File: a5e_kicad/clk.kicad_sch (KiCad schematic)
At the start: 20 parts, among them J1601 Conn_01x03_Pin, U1601 5P49V60A0000NL, Y1601 FOX FQ5225B-25

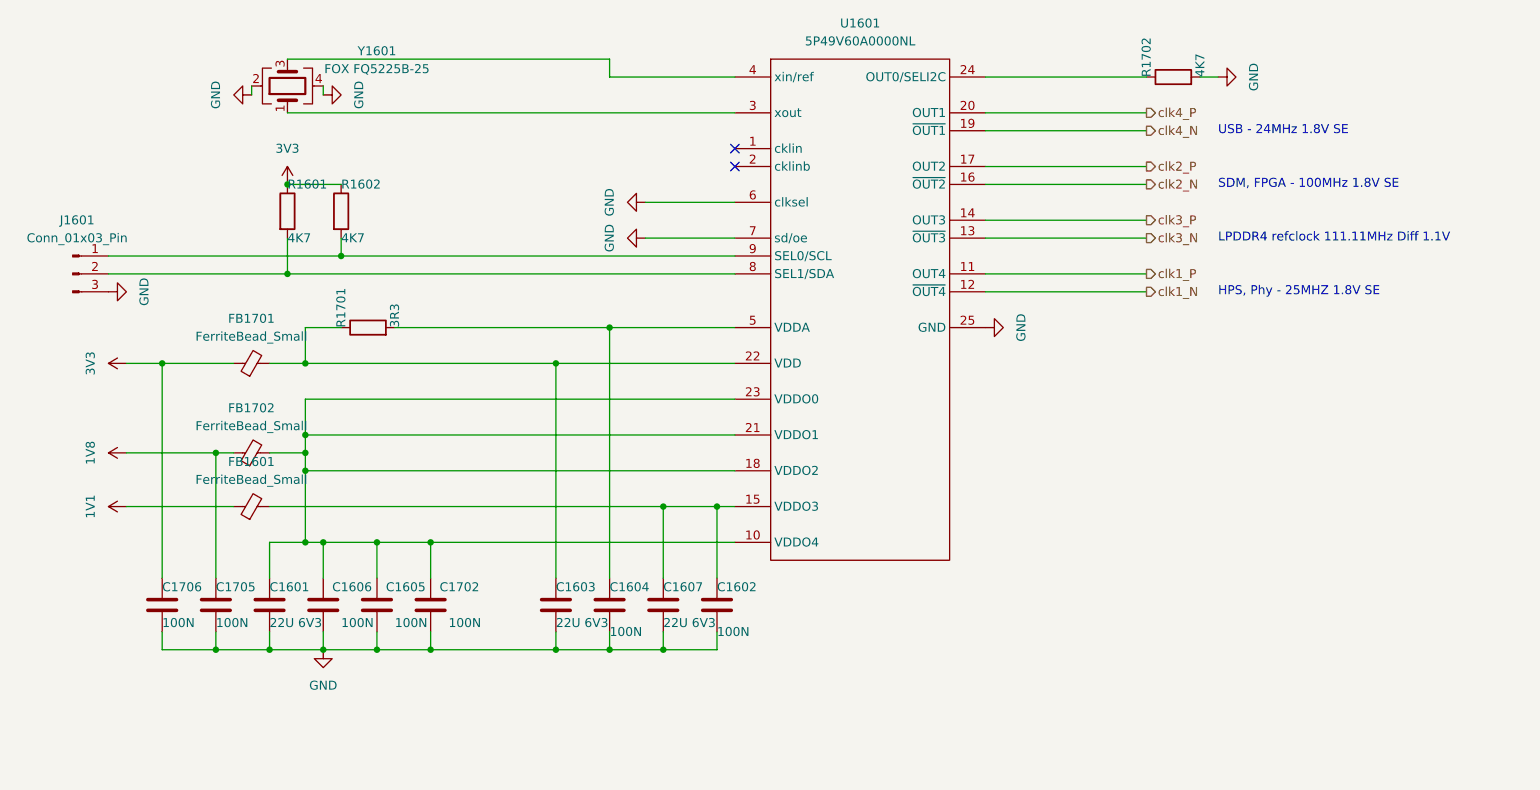
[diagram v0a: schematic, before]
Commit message: add vias to lppdr balls
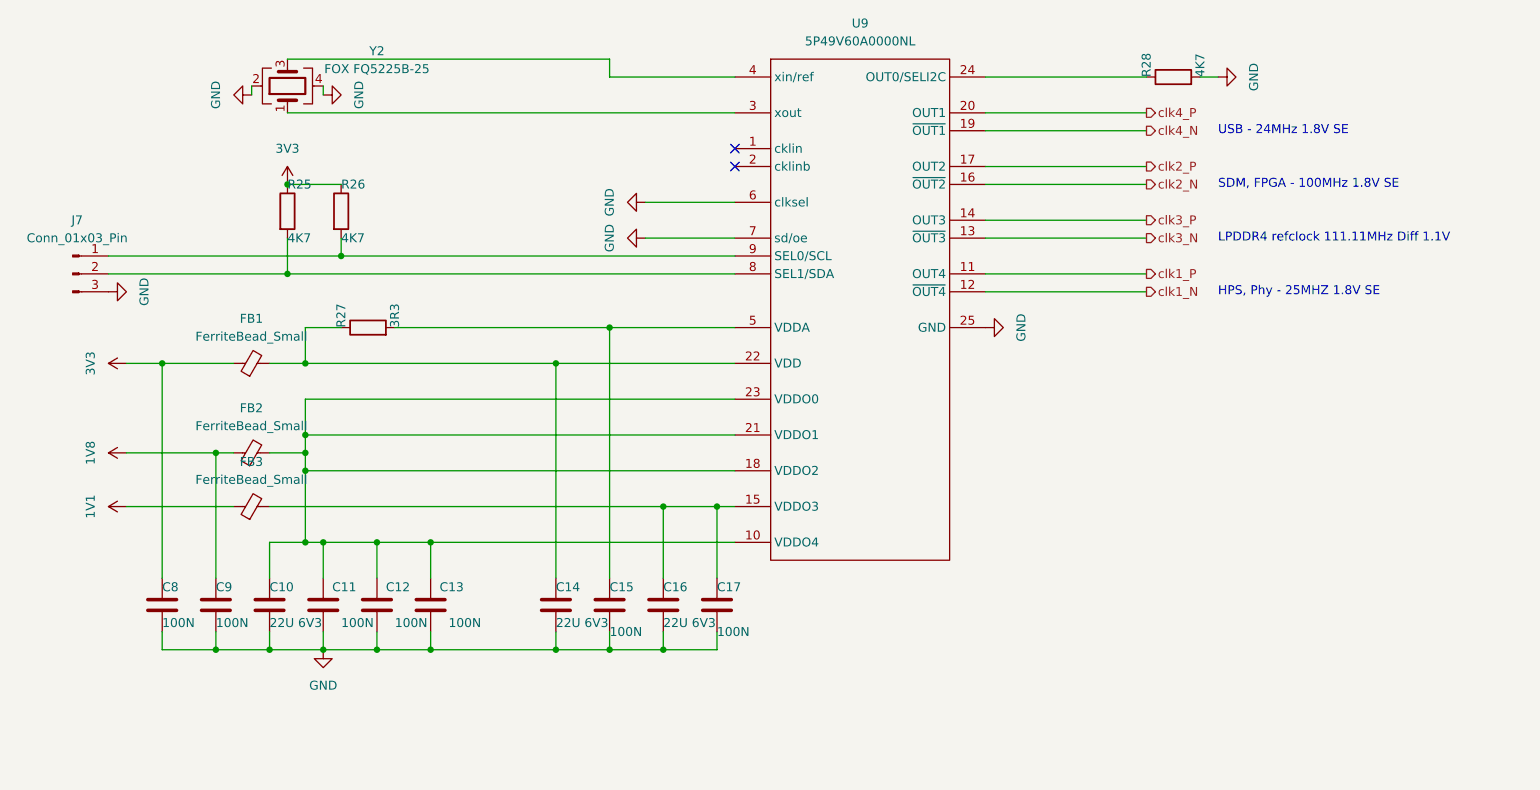
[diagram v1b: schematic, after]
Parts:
- renumbered C1601 to C10, C1606 to C11, C1605 to C12, C1702 to C13, C1603 to C14, C1604 to C15, C1607 to C16, C1602 to C17, C1706 to C8, C1705 to C9, FB1701 to FB1, FB1702 to FB2, FB1601 to FB3, J1601 to J7, R1601 to R25, R1602 to R26, R1701 to R27, R1702 to R28, U1601 to U9, Y1601 to Y2

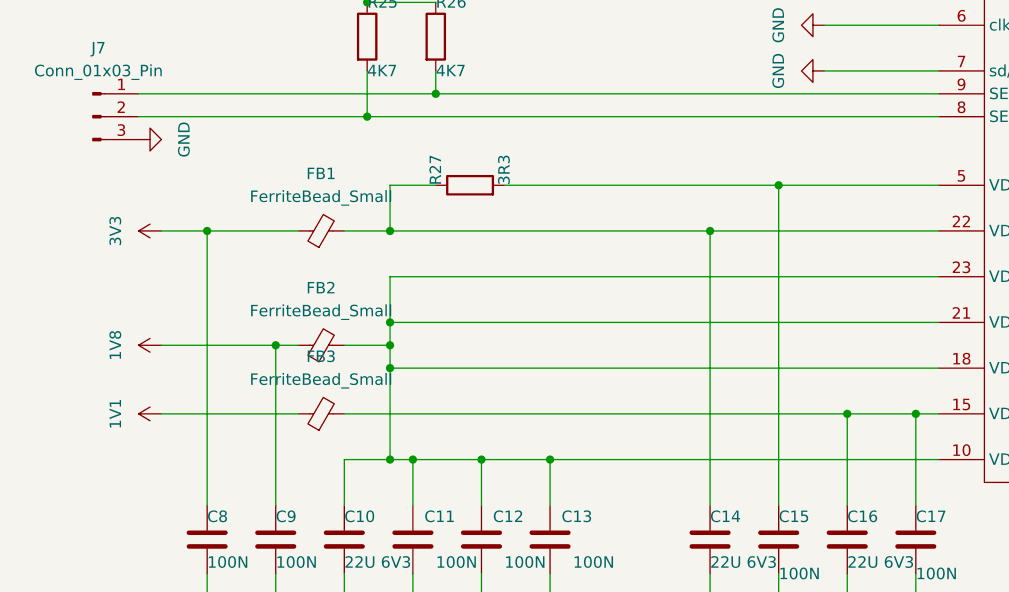
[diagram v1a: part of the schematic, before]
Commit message: add routes for power supplies
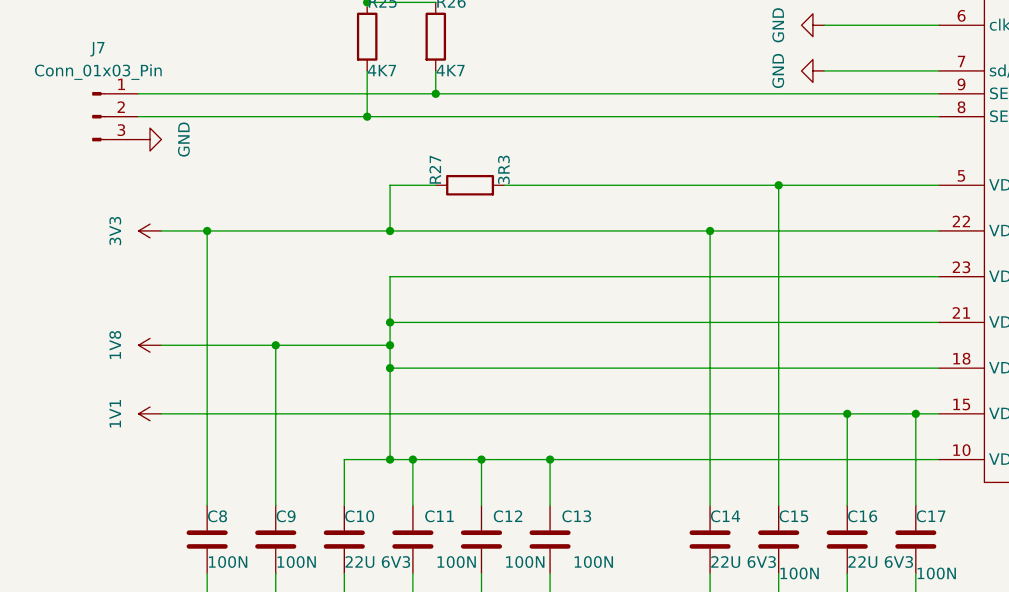
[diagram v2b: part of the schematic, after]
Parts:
- removed FB1, FB2, FB3: FerriteBead_Small, Capacitor_SMD:C_0603_1608Metric, symbol Device:FerriteBead_Small
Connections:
- net 1V1: now also C16.1, C17.1, U9.15 (VDDO3)
- net 1V8: now also C10.1, C11.1, C12.1, C13.1, U9.10 (VDDO4), U9.18 (VDDO2), U9.21 (VDDO1), U9.23 (VDDO0)
- net 3V3: now also C14.1, R27.1, U9.22 (VDD)

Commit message: savegame before trying to fix component names
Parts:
- added Y3: Si5351B-B-GM, Package_DFN_QFN:QFN-20-1EP_4x4mm_P0.5mm_EP2.7x2.7mm, symbol Oscillator:Si5351B-B-GM
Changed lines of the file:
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@@
+	)
+	(symbol
+		(lib_id "Oscillator:Si5351B-B-GM")
+		(at 212.09 113.03 0)
+		(unit 1)
+		(body_style 1)
+		(exclude_from_sim no)
+		(in_bom yes)
+		(on_board yes)
+		(in_pos_files yes)
+		(dnp no)
+		(fields_autoplaced yes)
+		(property "Reference" "Y3"
+			(at 214.2333 135.89 0)
+			(show_name no)
+			(do_not_autoplace no)
+			(effects
+				(font
+					(size 1.27 1.27)
+				)
+				(justify left)
+			)
+		)
+		(property "Value" "Si5351B-B-GM"
+			(at 214.2333 138.43 0)
+			(show_name no)
+			(do_not_autoplace no)
+			(effects
+				(font
+					(size 1.27 1.27)
+				)
+				(justify left)
+			)
+		)
+		(property "Footprint" "Package_DFN_QFN:QFN-20-1EP_4x4mm_P0.5mm_EP2.7x2.7mm"
+			(at 212.09 143.51 0)
+			(hide yes)
+			(show_name no)
+			(do_not_autoplace no)
+			(effects
+				(font
+					(size 1.27 1.27)
+				)
+			)
+		)
+		(property "Datasheet" "https://www.silabs.com/documents/public/data-sheets/Si5351-B.pdf"
+			(at 212.09 113.03 0)
+			(hide yes)
+			(show_name no)
+			(do_not_autoplace no)
+			(effects
+				(font
+					(size 1.27 1.27)
+				)
+			)
+		)
+		(property "Description" "I2C Programmable Any-Frequency CMOS Clock Generator + VCXO, QFN-20"
+			(at 212.09 113.03 0)
+			(hide yes)
+			(show_name no)
+			(do_not_autoplace no)
+			(effects
+				(font
+					(size 1.27 1.27)
+				)
+			)
+		)
+		(pin "2"
+		)
+		(pin "18"
+		)
+		(pin "21"
+		)
+		(pin "14"
+		)
+		(pin "6"
+		)
+		(pin "9"
+		)
+		(pin "1"
+		)
+		(pin "13"
+		)
+		(pin "10"
+		)
+		(pin "11"
+		)
+		(pin "5"
+		)
+		(pin "12"
+		)
+		(pin "16"
+		)
+		(pin "4"
+		)
+		(pin "15"
+		)
+		(pin "7"
+		)
+		(pin "3"
+		)
+		(pin "17"
+		)
+		(pin "19"
+		)
+		(pin "8"
+		)
+		(pin "20"
+		)
+		(instances
+			(project "agilex_3_soc"
+				(path "/a5b98d95-6877-4284-904f-d04e32723ae0/03ab2536-81c4-4b58-8998-1457d6fb7a1b"
+					(reference "Y3")
+					(unit 1)
+				)
+			)
+		)
 	)
 	(symbol

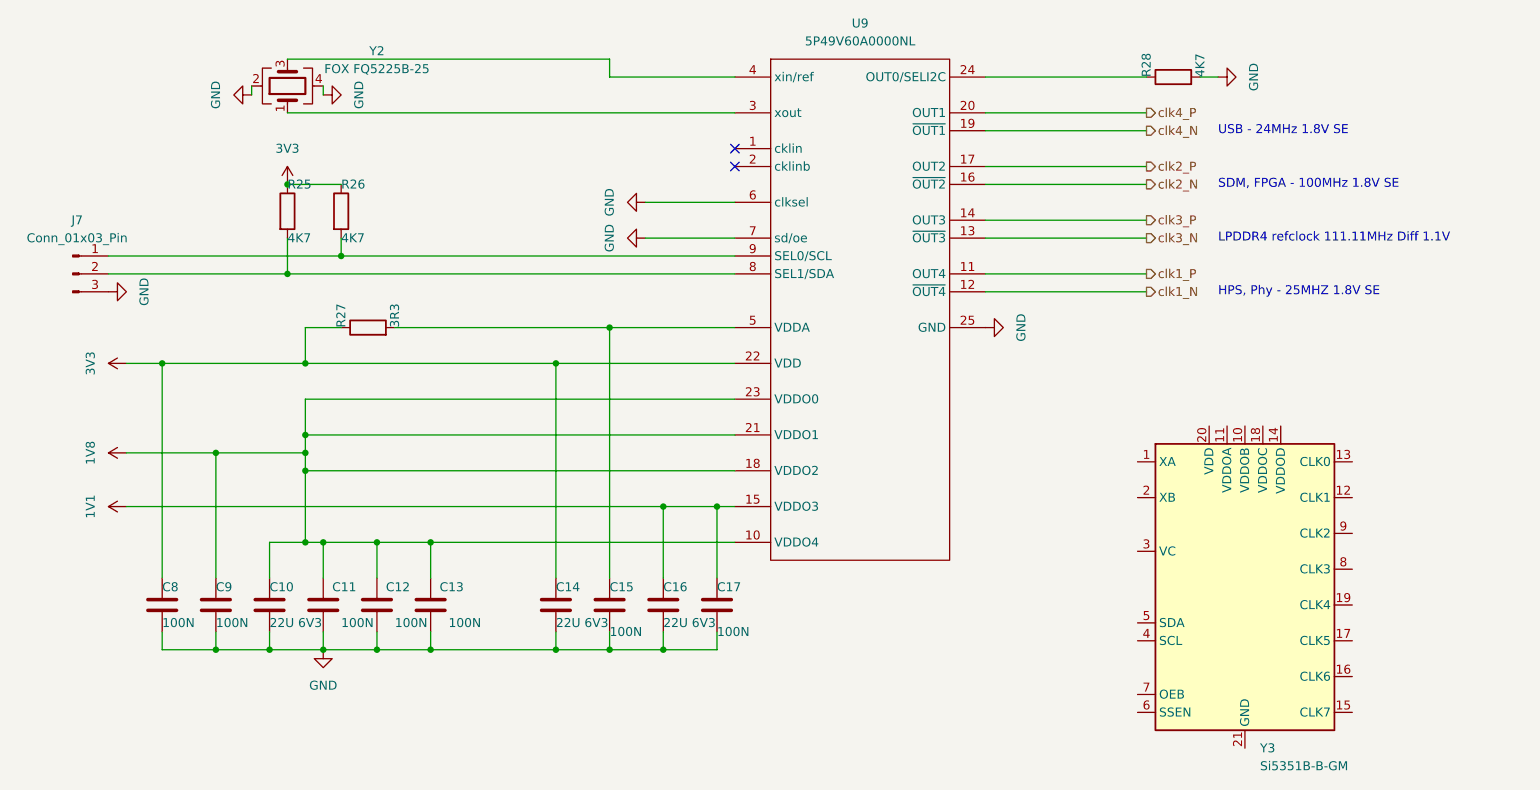
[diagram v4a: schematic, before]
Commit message: add separate clock ICs instead of using programmable ic
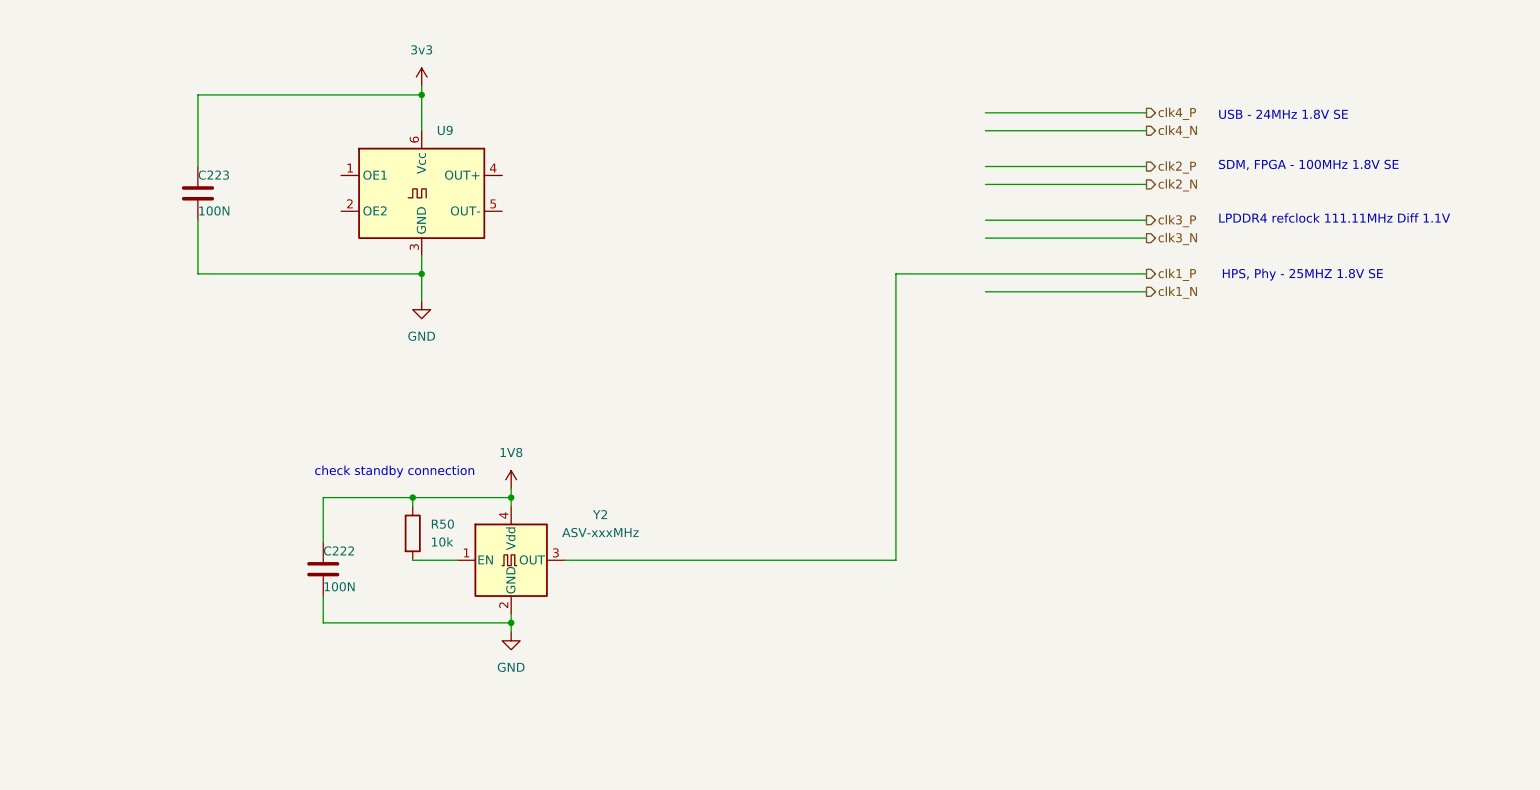
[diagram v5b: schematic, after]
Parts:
- removed C10, C14, C16: 22U 6V3, Capacitor_SMD:C_0402_1005Metric, symbol Device:C
- removed C11, C12, C13, C15, C17, C8, C9: 100N, Capacitor_SMD:C_0402_1005Metric, symbol Device:C
- removed J7: Conn_01x03_Pin, Connector_PinHeader_2.54mm:PinHeader_1x03_P2.54mm_Vertical, symbol Connector:Conn_01x03_Pin
- removed R25, R26, R28: 4K7, Resistor_SMD:R_0402_1005Metric, symbol Device:R
- removed R27: 3R3, Resistor_SMD:R_0402_1005Metric, symbol Device:R
- removed U9: 5P49V60A0000NL, Package_DFN_QFN:QFN-24-1EP_5x5mm_P0.65mm_EP3.25x3.25mm_ThermalVias, symbol PCAD_import:5P49V60A0000NL
- removed Y2: FOX FQ5225B-25, Oscillator:Oscillator_SMD_EuroQuartz_XO32-4Pin_3.2x2.5mm, symbol Device:Crystal_GND24
- removed Y3: Si5351B-B-GM, Package_DFN_QFN:QFN-20-1EP_4x4mm_P0.5mm_EP2.7x2.7mm, symbol Oscillator:Si5351B-B-GM
- added C222, C223: 100N, Capacitor_SMD:C_0201_0603Metric, symbol Device:C
- added R50: 10k, Resistor_SMD:R_0402_1005Metric, symbol Device:R
- added U9: (no value), symbol agilex_5_lib:XLL7
- added Y2: ASV-xxxMHz, Oscillator:Oscillator_SMD_Abracon_ASV-4Pin_7.0x5.1mm, symbol Oscillator:ASV-xxxMHz
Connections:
- net 1V8: now also C222.1, R50.1, Y2.4 (Vdd)
- net GND: now also C222.2, C223.2, U9.3 (GND), Y2.2 (GND)
- net clk1_P: now also Y2.3 (OUT)
- new net: R50.2, Y2.1 (EN)
- new net 3v3: C223.1, U9.6 (Vcc)
- no-connect marks 2 -> 0
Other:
- note added: "check standby connection"

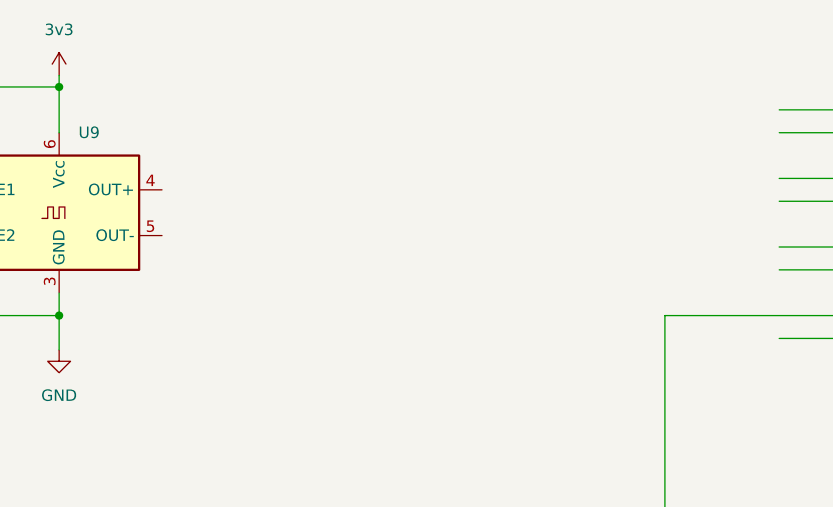
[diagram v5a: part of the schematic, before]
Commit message: add oscillator footprint and start adding ac biasing for lpddr clock
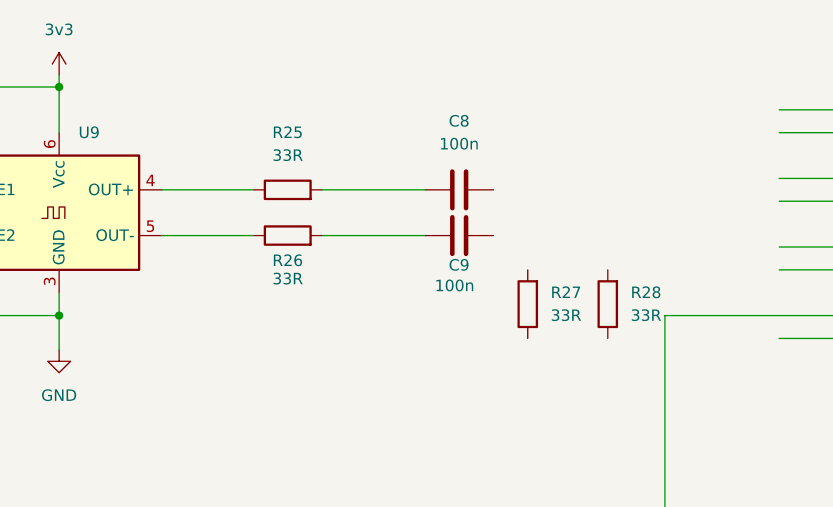
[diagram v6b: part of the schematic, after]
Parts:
- added C8, C9: 100n, symbol Device:C
- added R25, R26, R27, R28: 33R, symbol Device:R
- U9: footprint (none) -> agilex_lib:XL7
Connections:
- net at U9.4 (OUT+): now also R25.1
- net at U9.5 (OUT-): now also R26.1
- new net: C9.1, R26.2
- new net: C8.1, R25.2
